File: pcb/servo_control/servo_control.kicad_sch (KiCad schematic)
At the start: 62 parts, among them J1 Jack-DC, J10 Conn_01x03_Female, J11 Conn_01x03_Female, J12 Conn_01x03_Female, J13 Conn_01x03_Female, J14 Conn_01x03_Female, J15 Conn_01x03_Female, J16 Conn_01x03_Female, J17 Conn_01x03_Female, J18 Conn_01x03_Female, J19 Conn_01x03_Female, J2 YLIDAR X4, J20 Conn_01x03_Female, J21 Conn_01x06_Male, J22 GY-87, J3 Conn_01x03_Female, J4 Conn_01x03_Female, J5 Conn_01x03_Female, J6 Conn_01x03_Female, J7 Conn_01x03_Female, J8 Conn_01x03_Female, J9 Conn_01x03_Female, SW1 ESP_PROG, SW2 ESP_RST, U1 PCA9685PW, U2 LM317-3.3_SOT-223, U3 ESP32-WROOM-32, U4 MCP73213-A6SI/MF, U5 PCA9685PW, U6 LM317-5_SOT-223, U7 LT1085-ADJ

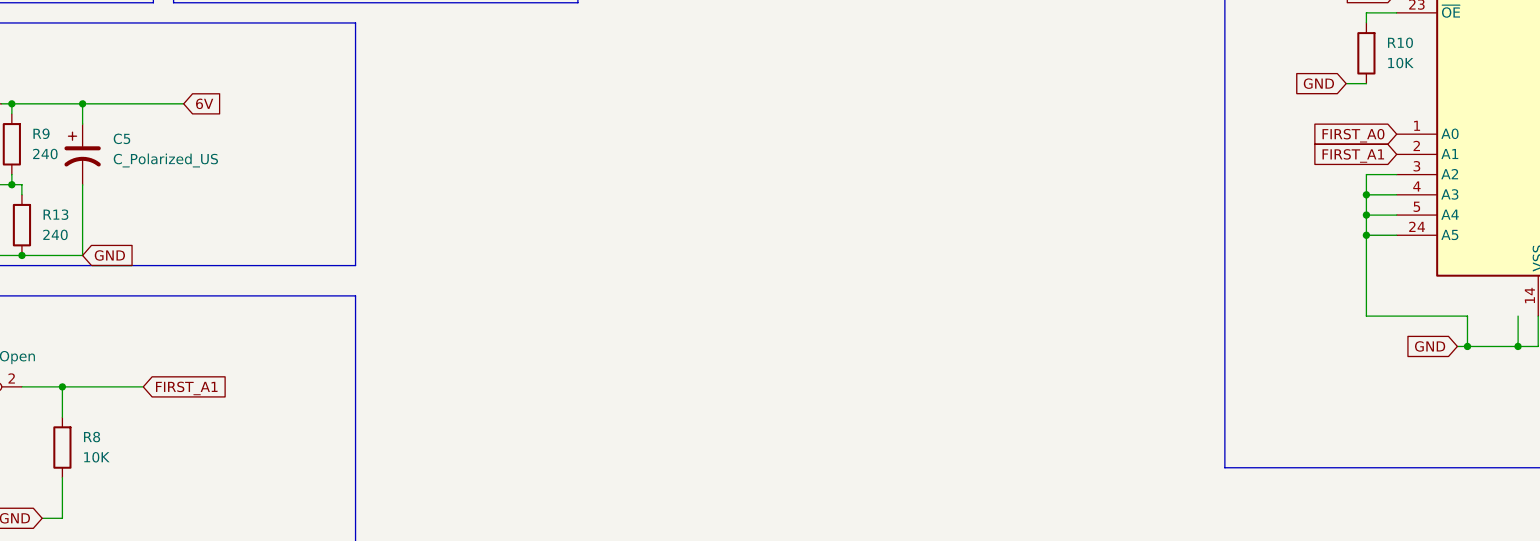
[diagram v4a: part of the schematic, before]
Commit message: update mcp9586 for i2c address
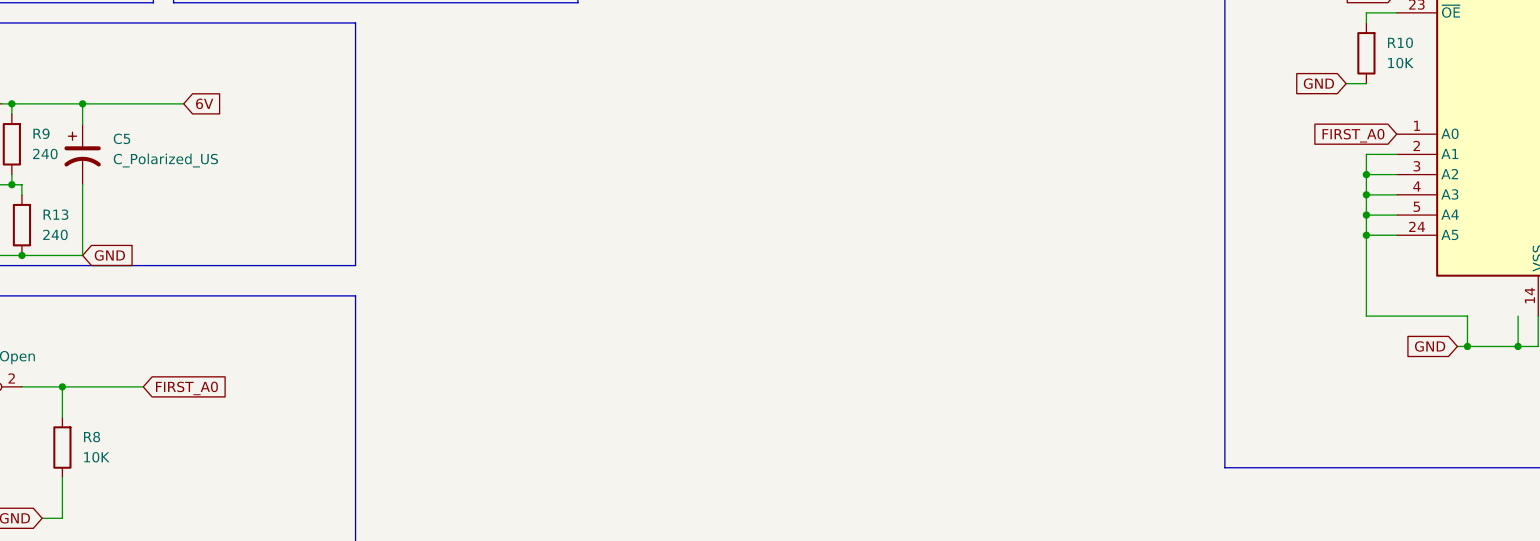
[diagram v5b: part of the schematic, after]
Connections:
- net FIRST_A0: now also JP2.2 (B), R8.2
- net GND: now also U1.2 (A1)
- removed net FIRST_A1: JP2.2 (B), R8.2, U1.2 (A1)
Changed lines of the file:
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@@
   (junction (at 96.52 237.49) (diameter 0) (color 0 0 0 0)
   )
+  (junction (at 217.17 64.77) (diameter 0) (color 0 0 0 0)
+  )
   (junction (at 193.04 232.41) (diameter 0) (color 0 0 0 0)
   )
@@
     (stroke (width 0) (type default) (color 0 0 0 0))
   )
+  (wire (pts (xy 220.98 62.23) (xy 217.17 62.23))
+    (stroke (width 0) (type default) (color 0 0 0 0))
+  )
   (wire (pts (xy 373.38 116.84) (xy 377.19 116.84))
     (stroke (width 0) (type default) (color 0 0 0 0))
@@
   )
   (polyline (pts (xy 199.39 15.24) (xy 199.39 101.6))
+    (stroke (width 0) (type default) (color 0 0 0 0))
+  )
+  (wire (pts (xy 217.17 62.23) (xy 217.17 64.77))
     (stroke (width 0) (type default) (color 0 0 0 0))
   )
@@
     )
   )
-  (global_label "FIRST_A1" (shape input) (at 63.5 91.44 0) (fields_autoplaced)
+  (global_label "FIRST_A0" (shape input) (at 63.5 91.44 0) (fields_autoplaced)
     (effects (font (size 1.27 1.27)) (justify left))
     (property "Intersheet References" "${INTERSHEET_REFS}" (id 0) (at 74.3193 91.3606 0)
@@
       (effects (font (size 1.27 1.27)) (justify right) hide)
     )
-  )
-  (global_label "FIRST_A1" (shape input) (at 220.98 62.23 180) (fields_autoplaced)
-    (effects (font (size 1.27 1.27)) (justify right))
-    (property "Intersheet References" "${INTERSHEET_REFS}" (id 0) (at 210.1607 62.3094 0)
-      (effects (font (size 1.27 1.27)) (justify right) hide)
-    )

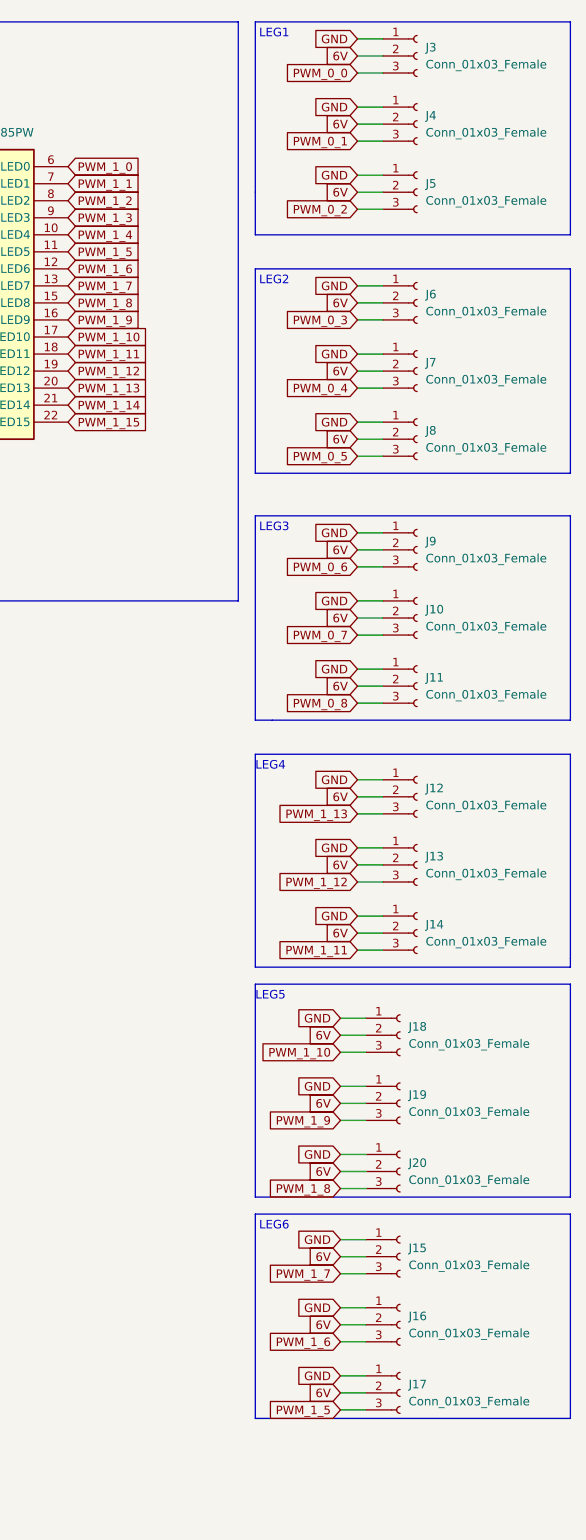
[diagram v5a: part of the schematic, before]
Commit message: add resistor current
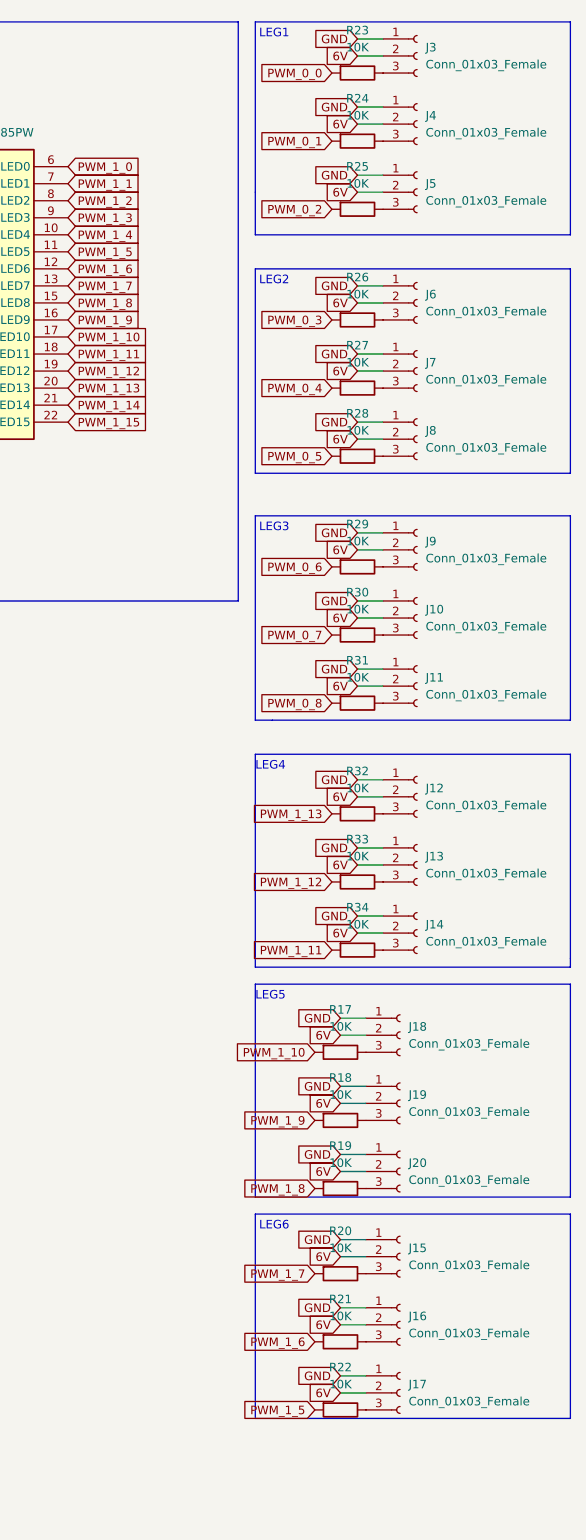
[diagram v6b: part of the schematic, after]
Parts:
- added R17, R18, R19, R20, R21, R22, R23, R24, R25, R26, R27, R28, R29, R30, R31, R32, R33, R34: 10K, Resistor_SMD:R_0603_1608Metric, symbol Device:R
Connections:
- net PWM_0_0: now also R23.2; no longer J3.3 (Pin_3)
- net PWM_0_1: now also R24.2; no longer J4.3 (Pin_3)
- net PWM_0_2: now also R25.2; no longer J5.3 (Pin_3)
- net PWM_0_3: now also R26.2; no longer J6.3 (Pin_3)
- net PWM_0_4: now also R27.2; no longer J7.3 (Pin_3)
- net PWM_0_5: now also R28.2; no longer J8.3 (Pin_3)
- net PWM_0_6: now also R29.2; no longer J9.3 (Pin_3)
- net PWM_0_7: now also R30.2; no longer J10.3 (Pin_3)
- net PWM_0_8: now also R31.2; no longer J11.3 (Pin_3)
- net PWM_1_10: now also R17.2; no longer J18.3 (Pin_3)
- net PWM_1_11: now also R34.2; no longer J14.3 (Pin_3)
- net PWM_1_12: now also R33.2; no longer J13.3 (Pin_3)
- net PWM_1_13: now also R32.2; no longer J12.3 (Pin_3)
- net PWM_1_5: now also R22.2; no longer J17.3 (Pin_3)
- net PWM_1_6: now also R21.2; no longer J16.3 (Pin_3)
- net PWM_1_7: now also R20.2; no longer J15.3 (Pin_3)
- net PWM_1_8: now also R19.2; no longer J20.3 (Pin_3)
- net PWM_1_9: now also R18.2; no longer J19.3 (Pin_3)
- new net: J4.3 (Pin_3), R24.1
- new net: J5.3 (Pin_3), R25.1
- new net: J18.3 (Pin_3), R17.1
- new net: J10.3 (Pin_3), R30.1
- new net: J6.3 (Pin_3), R26.1
- new net: J20.3 (Pin_3), R19.1
- new net: J8.3 (Pin_3), R28.1
- new net: J17.3 (Pin_3), R22.1
- new net: J13.3 (Pin_3), R33.1
- new net: J16.3 (Pin_3), R21.1
- new net: J19.3 (Pin_3), R18.1
- new net: J12.3 (Pin_3), R32.1
- new net: J9.3 (Pin_3), R29.1
- new net: J7.3 (Pin_3), R27.1
- new net: J11.3 (Pin_3), R31.1
- new net: J14.3 (Pin_3), R34.1
- new net: J3.3 (Pin_3), R23.1
- new net: J15.3 (Pin_3), R20.1

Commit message: pass servo control to atmega2560
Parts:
- removed R10, R11: 10K, Resistor_SMD:R_0603_1608Metric, symbol Device:R
- removed U1, U5: PCA9685PW, Package_SO:TSSOP-28_4.4x9.7mm_P0.65mm, symbol Driver_LED:PCA9685PW
- added U1: ATmega2560-16A, Package_QFP:TQFP-100_14x14mm_P0.5mm, symbol MCU_Microchip_ATmega:ATmega2560-16A
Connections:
- new net: U1.10 (VCC), U1.31 (VCC), U1.61 (VCC), U1.80 (VCC)
- new net: U1.11 (GND), U1.32 (GND), U1.62 (GND), U1.81 (GND), U1.99 (GND)
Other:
- note removed: "PCA9685_FIRST"
- note removed: "PCA9685_SECOND"

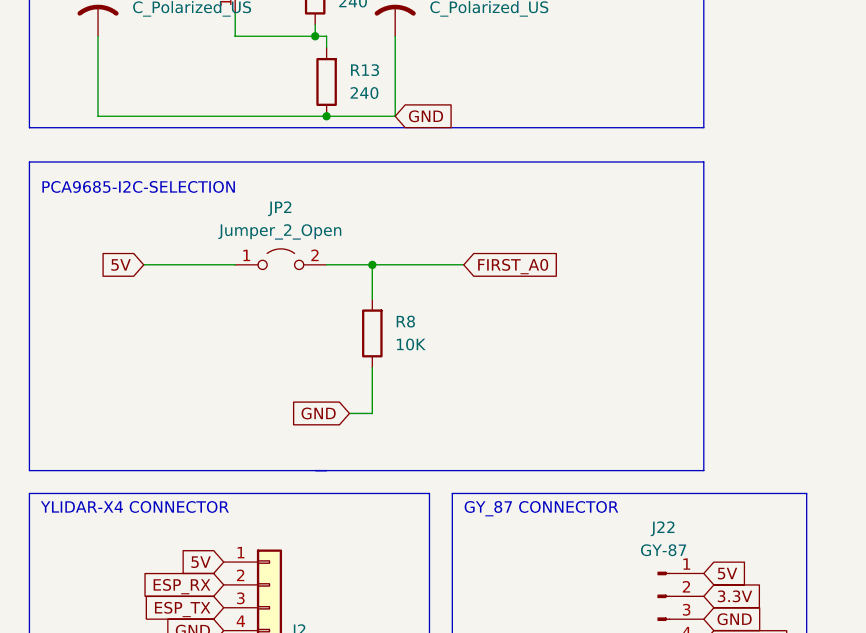
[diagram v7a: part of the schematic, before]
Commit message: add pcb atmega2560
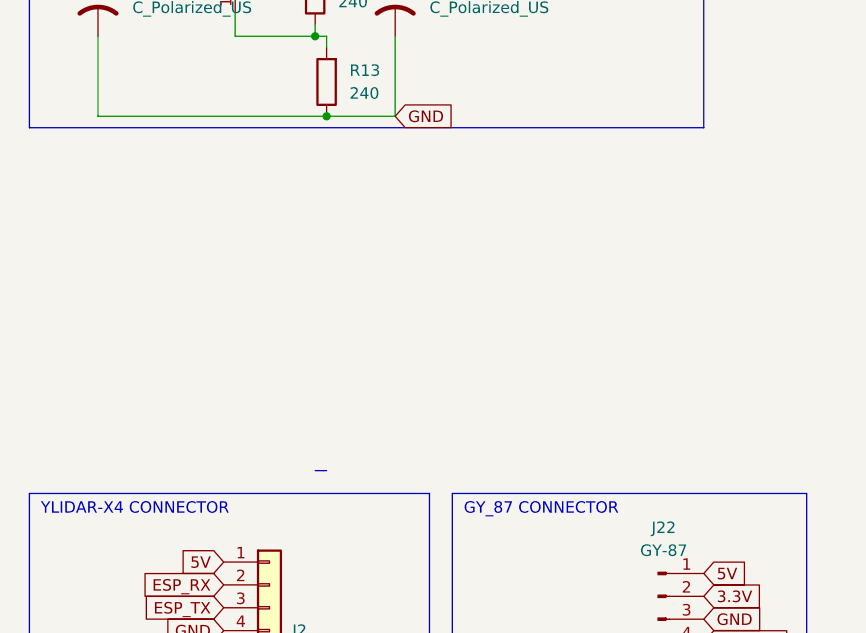
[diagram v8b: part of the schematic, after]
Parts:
- removed JP2: Jumper_2_Open, Jumper:SolderJumper-2_P1.3mm_Bridged2Bar_Pad1.0x1.5mm, symbol Jumper:Jumper_2_Open
- removed R8: 10K, Resistor_SMD:R_0603_1608Metric, symbol Device:R
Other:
- note removed: "PCA9685-I2C-SELECTION"
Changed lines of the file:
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@@
 (kicad_sch (version 20230121) (generator eeschema)
   (paper "A3")
-  (junction (at 53.34 91.44) (diameter 0) (color 0 0 0 0)
-  )
   (junction (at 46.99 66.04) (diameter 0) (color 0 0 0 0)
   )
@@
     (stroke (width 0) (type default))
   )
-  (polyline (pts (xy 15.24 80.01) (xy 15.24 114.3))
-    (stroke (width 0) (type default))
-  )
   (wire (pts (xy 373.38 30.48) (xy 377.19 30.48))
     (stroke (width 0) (type default))
@@
     (stroke (width 0) (type default))
   )
-  (polyline (pts (xy 48.26 114.3) (xy 90.17 114.3))
-    (stroke (width 0) (type default))
-  )
   (wire (pts (xy 96.52 229.87) (xy 96.52 237.49))
     (stroke (width 0) (type default))
@@
     (stroke (width 0) (type default))
   )
-  (wire (pts (xy 53.34 91.44) (xy 63.5 91.44))
-    (stroke (width 0) (type default))
-  )
   (wire (pts (xy 191.77 195.58) (xy 191.77 199.39))
     (stroke (width 0) (type default))
@@
     (stroke (width 0) (type default))
   )
-  (polyline (pts (xy 15.24 114.3) (xy 48.26 114.3))
-    (stroke (width 0) (type default))
-  )
   (wire (pts (xy 373.38 17.78) (xy 377.19 17.78))
     (stroke (width 0) (type default))
@@
     (stroke (width 0) (type default))
   )
-  (wire (pts (xy 27.94 91.44) (xy 38.1 91.44))
-    (stroke (width 0) (type default))
-  )
   (wire (pts (xy 90.17 201.93) (xy 90.17 204.47))
     (stroke (width 0) (type default))
@@
     (stroke (width 0) (type default))
   )
-  (wire (pts (xy 50.8 107.95) (xy 53.34 107.95))
-    (stroke (width 0) (type default))
-  )
   (wire (pts (xy 81.28 199.39) (xy 80.01 199.39))
     (stroke (width 0) (type default))
@@
     (stroke (width 0) (type default))
   )
-  (polyline (pts (xy 90.17 114.3) (xy 90.17 80.01))
-    (stroke (width 0) (type default))
-  )
   (wire (pts (xy 77.47 29.21) (xy 77.47 26.67))
     (stroke (width 0) (type default))
@@
     (stroke (width 0) (type default))
   )
-  (wire (pts (xy 48.26 91.44) (xy 53.34 91.44))
-    (stroke (width 0) (type default))
-  )
   (wire (pts (xy 191.77 199.39) (xy 193.04 199.39))
     (stroke (width 0) (type default))
@@
     (stroke (width 0) (type default))
   )
-  (wire (pts (xy 53.34 102.87) (xy 53.34 107.95))
-    (stroke (width 0) (type default))
-  )
   (wire (pts (xy 104.14 204.47) (xy 109.22 204.47))
     (stroke (width 0) (type default))
@@
     (stroke (width 0) (type default))
   )
-  (wire (pts (xy 53.34 91.44) (xy 53.34 95.25))
-    (stroke (width 0) (type default))
-  )
   (wire (pts (xy 370.84 219.71) (xy 374.65 219.71))
     (stroke (width 0) (type default))
@@
     (stroke (width 0) (type default))
   )
-  (polyline (pts (xy 90.17 80.01) (xy 15.24 80.01))
-    (stroke (width 0) (type default))
-  )
   (polyline (pts (xy 62.23 116.84) (xy 101.6 116.84))
     (stroke (width 0) (type default))
@@
     (effects (font (size 1.27 1.27)) (justify left bottom))
   )
-  (text "PCA9685-I2C-SELECTION" (at 16.51 83.82 0)
-    (effects (font (size 1.27 1.27)) (justify left bottom))
-  )
   (text "LEG6\n" (at 363.22 195.58 0)
     (effects (font (size 1.27 1.27)) (justify right bottom))
@@
     )
   )
-  (global_label "FIRST_A0" (shape input) (at 63.5 91.44 0) (fields_autoplaced)
-    (effects (font (size 1.27 1.27)) (justify left))
-    (property "Intersheetrefs" "${INTERSHEET_REFS}" (at 74.3193 91.3606 0)
-      (effects (font (size 1.27 1.27)) (justify left) hide)
-    )
-  )
   (global_label "GND" (shape input) (at 373.38 74.93 180) (fields_autoplaced)
     (effects (font (size 1.27 1.27)) (justify right))
@@
     )
   )
-  (global_label "5V" (shape input) (at 27.94 91.44 180) (fields_autoplaced)
-    (effects (font (size 1.27 1.27)) (justify right))
-    (property "Intersheetrefs" "${INTERSHEET_REFS}" (at 23.2288 91.3606 0)
-      (effects (font (size 1.27 1.27)) (justify right) hide)
-    )
-  )
   (global_label "GND" (shape input) (at 140.97 234.95 0) (fields_autoplaced)
     (effects (font (size 1.27 1.27)) (justify left))
@@
     )
   )
-  (global_label "GND" (shape input) (at 50.8 107.95 180) (fields_autoplaced)
-    (effects (font (size 1.27 1.27)) (justify right))
-    (property "Intersheetrefs" "${INTERSHEET_REFS}" (at 44.5164 107.8706 0)
-      (effects (font (size 1.27 1.27)) (justify right) hide)
-    )
-  )
   (global_label "GND" (shape input) (at 373.38 138.43 180) (fields_autoplaced)
     (effects (font (size 1.27 1.27)) (justify right))
@@
     )
   )
-  (symbol (lib_id "Jumper:Jumper_2_Open") (at 43.18 91.44 0) (unit 1)
-    (in_bom yes) (on_board yes) (dnp no) (fields_autoplaced)
-    (property "Reference" "JP2" (at 43.18 85.09 0)
-      (effects (font (size 1.27 1.27)))
-    )
-    (property "Value" "Jumper_2_Open" (at 43.18 87.63 0)
-      (effects (font (size 1.27 1.27)))
-    )
-    (property "Footprint" "Jumper:SolderJumper-2_P1.3mm_Bridged2Bar_Pad1.0x1.5mm" (at 43.18 91.44 0)
-      (effects (font (size 1.27 1.27)) hide)
-    )
-    (property "Datasheet" "~" (at 43.18 91.44 0)
-      (effects (font (size 1.27 1.27)) hide)
-    )
-    (pin "1")
-    (pin "2")
-    (instances
-      (project "servo_control"
-        (path "/dcee87eb-58b7-46fe-9143-b216c98d2b37"
-          (reference "JP2") (unit 1)
-        )
-      )
-    )
-  )
   (symbol (lib_id "Device:R") (at 109.22 248.92 90) (unit 1)
     (in_bom yes) (on_board yes) (dnp no)
@@
         )
       )
-    )
-  )
-  (symbol (lib_id "Device:R") (at 53.34 99.06 180) (unit 1)
-    (in_bom yes) (on_board yes) (dnp no) (fields_autoplaced)
-    (property "Reference" "R8" (at 55.88 97.7899 0)
-      (effects (font (size 1.27 1.27)) (justify right))
-    )
-    (property "Value" "10K" (at 55.88 100.3299 0)
-      (effects (font (size 1.27 1.27)) (justify right))
-    )
-    (property "Footprint" "Resistor_SMD:R_0603_1608Metric" (at 55.118 99.06 90)
-      (effects (font (size 1.27 1.27)) hide)
-    )
-    (property "Datasheet" "~" (at 53.34 99.06 0)
-      (effects (font (size 1.27 1.27)) hide)
-    )
-    (pin "1")
-    (pin "2")
-    (instances
-      (project "servo_control"
-        (path "/dcee87eb-58b7-46fe-9143-b216c98d2b37"
-          (reference "R8") (unit 1)
-        )
-      )
